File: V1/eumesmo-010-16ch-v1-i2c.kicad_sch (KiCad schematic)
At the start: 42 parts, among them U10 ISO1540, U11 PCA9685PW, U12 MCP23017

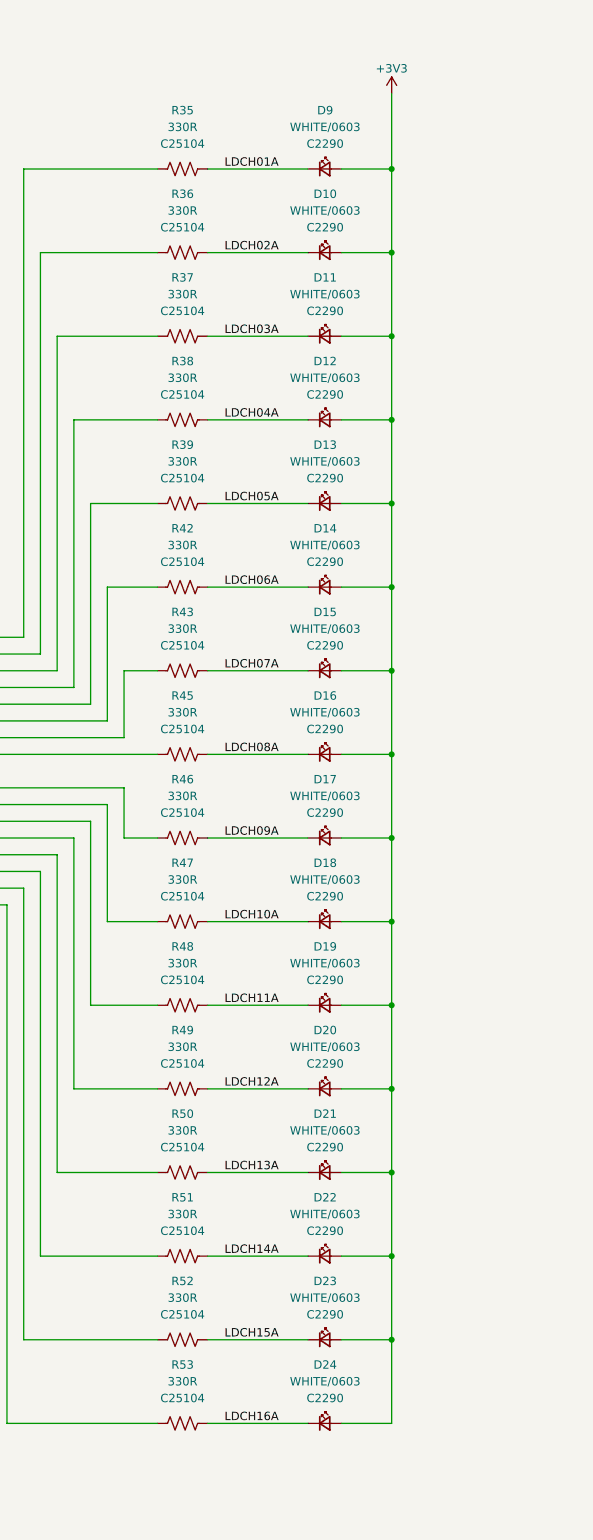
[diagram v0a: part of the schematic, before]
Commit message: Change LEDs for orange
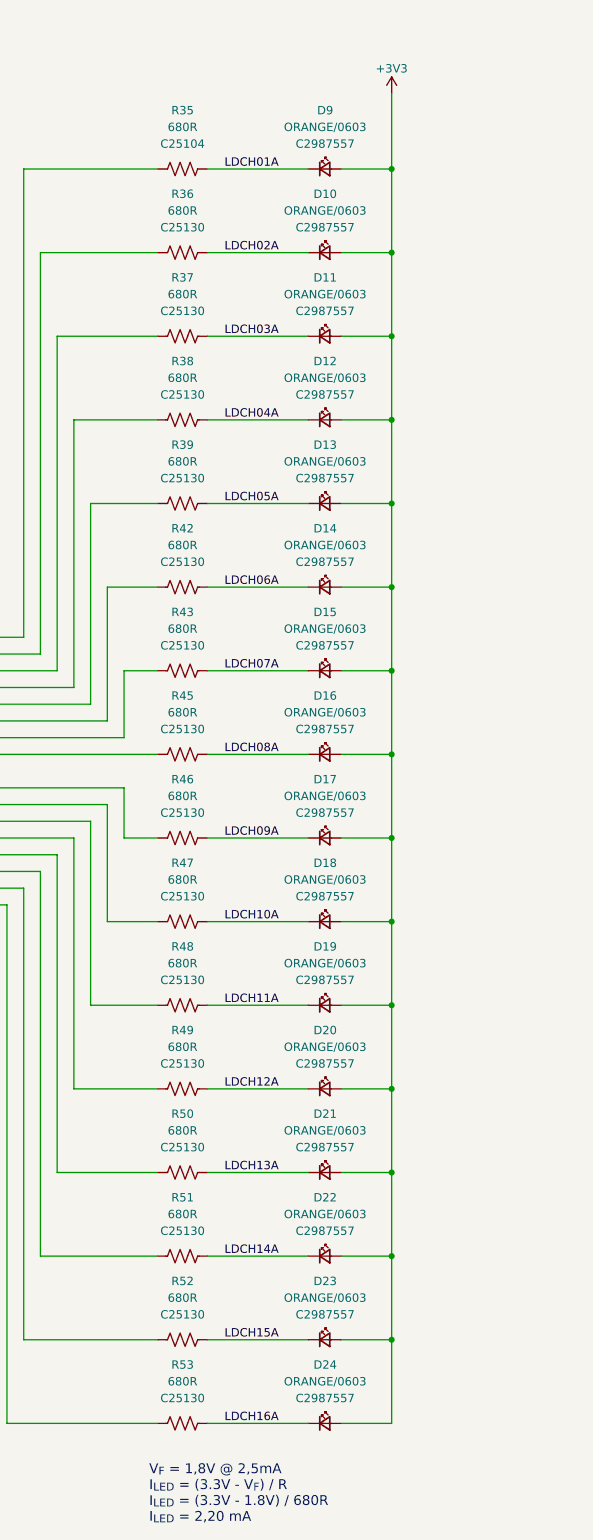
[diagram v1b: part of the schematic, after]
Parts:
- D10, D11, D12, D13, D14, D15, D16, D17, D18, D19, D20, D21, D22, D23, D24, D9: value WHITE/0603 -> ORANGE/0603; LCSC Part # C2290 -> C2987557; Mfr Hubei KENTO Elec -> Everlight Elec; Mfr PN KT-0603W -> 19-217/S2C-AL1M2VY/6T; Vendor PN C2290 -> C2987557
- R35: value 330R -> 680R
- R36, R37, R38, R39, R42, R43, R45, R46, R47, R48, R49, R50, R51, R52, R53: value 330R -> 680R; LCSC Part # C25104 -> C25130; Mfr PN 0402WGF3300TCE -> 0402WGF6800TCE; Vendor PN C25104 -> C25130
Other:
- note added: "V_{F} = 1,8V @ 2,5mA I_{LED} = (3.3V - V_{F}) / R I_{LED} = (3.3V - 1.8V) / 680R I_{LED} = 2,20 mA"

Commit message: Component rotations and offsets ajusted for JLCPCB
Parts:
- R35: LCSC Part # C25104 -> C25130; Mfr PN 0402WGF3300TCE -> 0402WGF6800TCE; Vendor PN C25104 -> C25130
- U11: FT Rotation Offset (none) -> 90
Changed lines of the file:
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@@
 			)
 		)
-		(property "LCSC Part #" "C25104"
+		(property "LCSC Part #" "C25130"
 			(at 137.16 63.5 90)
 			(show_name no)
@@
 			)
 		)
-		(property "Mfr PN" "0402WGF3300TCE"
+		(property "Mfr PN" "0402WGF6800TCE"
 			(at 137.16 67.31 0)
 			(hide yes)
@@
 			)
 		)
-		(property "Vendor PN" "C25104"
+		(property "Vendor PN" "C25130"
 			(at 137.16 67.31 0)
 			(hide yes)
@@
 			(at 345.44 146.05 0)
 			(hide yes)
+			(show_name no)
+			(do_not_autoplace no)
+			(effects
+				(font
+					(size 1.27 1.27)
+				)
+			)
+		)
+		(property "FT Rotation Offset" "90"
+			(at 345.44 146.05 0)
+			(hide yes)
